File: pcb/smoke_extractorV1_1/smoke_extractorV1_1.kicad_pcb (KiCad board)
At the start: 2 copper layers, 54 x 27 mm, 43 parts, among them J1 USB_C_Receptacle, J2 Screw_Terminal_01x02, Q1 AO3400A, U1 LMV331, U2 RA11131100, U3 MP1542, U4 LMV331, U5 LMV331

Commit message: Version 1.2
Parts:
- added D6: SS34, Diode_SMD:Nexperia_CFP3_SOD-123W, F.Cu at (98.6, 111.5)
- added kibuzzard-631C7DF6: G***, kibuzzard-631C7DF6, F.Cu at (144.5, 107.0)
- added kibuzzard-631C7E0D: G***, kibuzzard-631C7E0D, F.Cu at (144.6, 112.0)
- R10: value 4k7 -> 5k1
- R12: value 86.6k -> 1k
- R17: value 10k -> 12k
- R18, R19, R6: value 4.7k -> 5k1
- R5: value 4.7k -> 47k
- R9: value 330 -> 100
- U1, U4, U5: footprint Package_TO_SOT_SMD:SOT-353_SC-70-5_Handsoldering -> Package_TO_SOT_SMD:SOT-23-5_HandSoldering
- moved R15 3.79 mm to (115.9, 98.6), turned to 90 degrees
- moved R8 0.91 mm to (94.6, 114.1), turned to -90 degrees
- moved R7 0.81 mm to (97.5, 115.0), turned to 0 degrees
- moved R9 0.45 mm to (107.0, 113.5)
- moved C7 0.21 mm to (119.7, 109.3)
- moved R14 0.06 mm to (117.8, 102.4)
- turned Q1 to 90 degrees
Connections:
- C1 pad 1: VBUS_RAW -> VBUS_OPEN
- C2 pad 2: GND -> VBUS_DRAIN
- C3 pad 2: GND -> VBUS_DRAIN
- C5 pad 2: GND -> VBUS_DRAIN
- C6 pad 1: VBUS_RAW -> VBUS_OPEN
- C7 pad 1: VBUS_RAW -> VBUS_OPEN
- D4 pad 1: GND -> VBUS_DRAIN
- J1 pad A4: VBUS_RAW -> VBUS_OPEN
- J1 pad A9: VBUS_RAW -> VBUS_OPEN
- J1 pad B4: VBUS_RAW -> VBUS_OPEN
- J1 pad B9: VBUS_RAW -> VBUS_OPEN
- J2 pad 2: GND -> VBUS_DRAIN
- Q1 pad 2: VBUS_OPEN -> GND
- Q1 pad 3: VBUS_RAW -> VBUS_DRAIN
- R1 pad 2: VBUS_RAW -> VBUS_OPEN
- R14 pad 2: GND -> VBUS_DRAIN
- R15 pad 2: GND -> VBUS_DRAIN
- R17 pad 2: GND -> VBUS_DRAIN
- R18 pad 2: VBUS_RAW -> VBUS_OPEN
- R19 pad 2: VBUS_RAW -> VBUS_OPEN
- R3 pad 2: VBUS_RAW -> VBUS_OPEN
- R6 pad 2: VBUS_RAW -> VBUS_OPEN
- R7 pad 2: VBUS_RAW -> VBUS_OPEN
- U1 pad 5: VBUS_RAW -> VBUS_OPEN
- U3 pad 4: GND -> VBUS_DRAIN
- U4 pad 5: VBUS_RAW -> VBUS_OPEN
- U5 pad 5: VBUS_RAW -> VBUS_OPEN
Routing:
- net VBUS_RAW: track 28.3 -> 0.00 mm, vias 3 -> 0
- net VBUS_OPEN: track 0.00 -> 24.6 mm, vias 0 -> 3
- net Net-(Q1-Pad1): track 0.00 -> 8.23 mm
- net V_CC_REF: track 40.9 -> 44.2 mm
- net CHG_DET: track 15.4 -> 16.4 mm
- net Net-(C4-Pad2): track 2.12 -> 2.72 mm
- net VBUS_DRAIN: vias 0 -> 28
- net GND: vias 162 -> 125
- added copper zone on B.Cu, net VBUS_DRAIN
- added copper zone on F.Cu, net VBUS_DRAIN
- removed copper zone on F.Cu, net Net-(Q1-Pad1)
- removed copper zone on F.Cu, net VBUS_RAW
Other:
- board text added: "Nuno Nogueira Stockholm Set 2022"
- board text added: "Smoke Extractor 1v2"
- board text removed: "Nuno Nogueira Stockholm July 2022"
- board text removed: "Smoke Extractor 1v1"

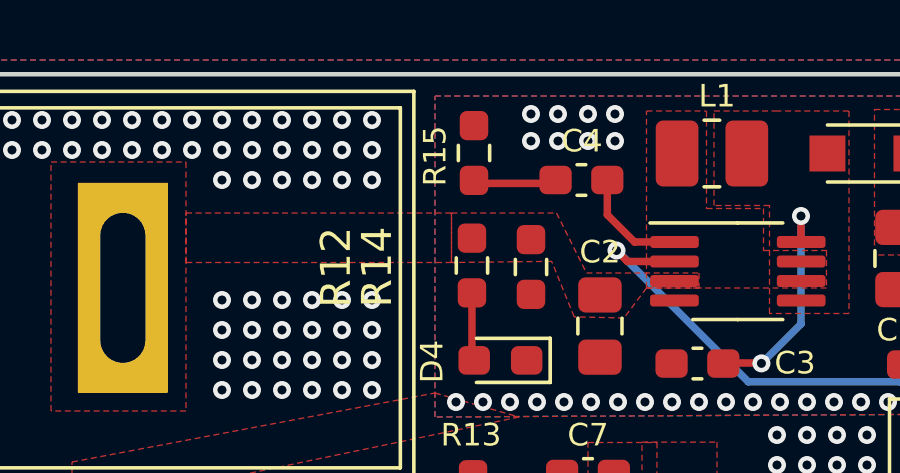
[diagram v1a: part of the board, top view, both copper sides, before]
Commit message: Added testing pads for version 1.2
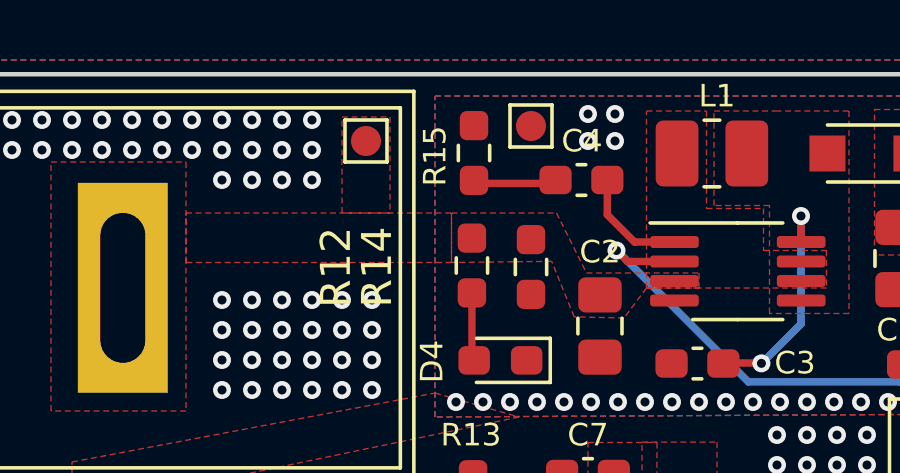
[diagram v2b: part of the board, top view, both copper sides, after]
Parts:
- added REF**: TestPoint_Pad_1.0x1.0mm, TestPoint:TestPoint_Pad_1.0x1.0mm, F.Cu at (112.3, 98.2)
- added REF**: TestPoint_Pad_1.0x1.0mm, TestPoint:TestPoint_Pad_1.0x1.0mm, F.Cu at (117.8, 97.7)
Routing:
- net VBUS_DRAIN: vias 28 -> 24
- net GND: vias 125 -> 119
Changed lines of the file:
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@@
     )
+  )
+  (footprint "TestPoint:TestPoint_Pad_1.0x1.0mm" (layer "F.Cu")
+    (at 112.3 98.2)
+    (descr "SMD rectangular pad as test Point, square 1.0mm side length")
+    (tags "test point SMD pad rectangle square")
+    (attr exclude_from_pos_files exclude_from_bom)
+    (fp_text reference "REF**" (at 0 -1.448) (layer "F.SilkS") hide
+      (effects (font (size 1 1) (thickness 0.15)))
+    )
+    (fp_text value "TestPoint_Pad_1.0x1.0mm" (at 0 1.55) (layer "F.Fab") hide
+      (effects (font (size 1 1) (thickness 0.15)))
+    )
+    (fp_text user "${REFERENCE}" (at 0 -1.45) (layer "F.Fab") hide
+      (effects (font (size 1 1) (thickness 0.15)))
+    )
+    (fp_line (start -0.7 0.7) (end -0.7 -0.7) (layer "F.SilkS") (width 0.12))
+    (fp_line (start 0.7 0.7) (end -0.7 0.7) (layer "F.SilkS") (width 0.12))
+    (fp_line (start -0.7 -0.7) (end 0.7 -0.7) (layer "F.SilkS") (width 0.12))
+    (fp_line (start 0.7 -0.7) (end 0.7 0.7) (layer "F.SilkS") (width 0.12))
+    (fp_line (start 1 1) (end -1 1) (layer "F.CrtYd") (width 0.05))
+    (fp_line (start 1 1) (end 1 -1) (layer "F.CrtYd") (width 0.05))
+    (fp_line (start -1 -1) (end 1 -1) (layer "F.CrtYd") (width 0.05))
+    (fp_line (start -1 -1) (end -1 1) (layer "F.CrtYd") (width 0.05))
+    (pad "1" smd circle (at 0 0) (size 1 1) (layers "F.Cu" "F.Mask")
+      (net 2 "VBUS_SWITCH") (zone_connect 2))
   )
   (footprint "Capacitor_SMD:C_0603_1608Metric_Pad1.08x0.95mm_HandSolder" locked (layer "F.Cu")
@@
     (attr board_only exclude_from_pos_files exclude_from_bom)
     (fp_text reference "kibuzzard-631C7E0D" (at 0 -3.511021 90) (layer "F.SilkS") hide
-      (effects (font (size 0 0)))
+      (effects (font (size 0 0) (thickness 0.15)))
     )
     (fp_text value "G***" (at 0 3.511021 90) (layer "F.SilkS") hide
-      (effects (font (size 0 0)))
+      (effects (font (size 0 0) (thickness 0.15)))
     )
     (fp_poly (pts
@@
     (attr board_only exclude_from_pos_files exclude_from_bom)
     (fp_text reference "kibuzzard-631C7DF6" (at 0 -3.511021 90) (layer "F.SilkS") hide
-      (effects (font (size 0 0)))
+      (effects (font (size 0 0) (thickness 0.15)))
     )
     (fp_text value "G***" (at 0 3.511021 90) (layer "F.SilkS") hide
-      (effects (font (size 0 0)))
+      (effects (font (size 0 0) (thickness 0.15)))
     )
     (fp_poly (pts
@@
     )
   )
+  (footprint "TestPoint:TestPoint_Pad_1.0x1.0mm" (layer "F.Cu")
+    (at 117.8 97.7)
+    (descr "SMD rectangular pad as test Point, square 1.0mm side length")
+    (tags "test point SMD pad rectangle square")
+    (attr exclude_from_pos_files exclude_from_bom)
+    (fp_text reference "REF**" (at 0 -1.448) (layer "F.SilkS") hide
+      (effects (font (size 1 1) (thickness 0.15)))
+    )
+    (fp_text value "TestPoint_Pad_1.0x1.0mm" (at 0 1.55) (layer "F.Fab") hide
+      (effects (font (size 1 1) (thickness 0.15)))
+    )
+    (fp_text user "${REFERENCE}" (at 0 -1.45) (layer "F.Fab") hide
+      (effects (font (size 1 1) (thickness 0.15)))
+    )
+    (fp_line (start 0.7 0.7) (end -0.7 0.7) (layer "F.SilkS") (width 0.12))
+    (fp_line (start -0.7 -0.7) (end 0.7 -0.7) (layer "F.SilkS") (width 0.12))
+    (fp_line (start -0.7 0.7) (end -0.7 -0.7) (layer "F.SilkS") (width 0.12))
+    (fp_line (start 0.7 -0.7) (end 0.7 0.7) (layer "F.SilkS") (width 0.12))
+    (fp_line (start 1 1) (end 1 -1) (layer "F.CrtYd") (width 0.05))
+    (fp_line (start -1 -1) (end 1 -1) (layer "F.CrtYd") (width 0.05))
+    (fp_line (start 1 1) (end -1 1) (layer "F.CrtYd") (width 0.05))
+    (fp_line (start -1 -1) (end -1 1) (layer "F.CrtYd") (width 0.05))
+    (pad "1" smd circle (at 0 0) (size 1 1) (layers "F.Cu" "F.Mask")
+      (net 24 "VBUS_DRAIN") (zone_connect 2))
+  )
   (footprint "Diode_SMD:D_SOD-523" locked (layer "F.Cu")
     (at 110.55 114.45)
@@
   (via locked (at 137.5 97.5) (size 0.6) (drill 0.3) (layers "F.Cu" "B.Cu") (free) (net 1))
   (via locked (at 108.5 103.5) (size 0.6) (drill 0.3) (layers "F.Cu" "B.Cu") (free) (net 1))
-  (via locked (at 112.5 99.5) (size 0.6) (drill 0.3) (layers "F.Cu" "B.Cu") (free) (net 1))
   (via locked (at 126 110) (size 0.6) (drill 0.3) (layers "F.Cu" "B.Cu") (free) (net 1))
   (via locked (at 103.5 98.5) (size 0.6) (drill 0.3) (layers "F.Cu" "B.Cu") (free) (net 1))
-  (via locked (at 111.5 98.5) (size 0.6) (drill 0.3) (layers "F.Cu" "B.Cu") (free) (net 1))
   (via locked (at 139.5 102.5) (size 0.6) (drill 0.3) (layers "F.Cu" "B.Cu") (free) (net 1))
   (via locked (at 136.5 114) (size 0.6) (drill 0.3) (layers "F.Cu" "B.Cu") (free) (net 1))
@@
   (via locked (at 137.5 99.5) (size 0.6) (drill 0.3) (layers "F.Cu" "B.Cu") (free) (net 1))
   (via locked (at 109.5 99.5) (size 0.6) (drill 0.3) (layers "F.Cu" "B.Cu") (free) (net 1))
-  (via locked (at 112.5 97.5) (size 0.6) (drill 0.3) (layers "F.Cu" "B.Cu") (free) (net 1))
   (via locked (at 129 109) (size 0.6) (drill 0.3) (layers "F.Cu" "B.Cu") (free) (net 1))
   (via locked (at 127 110) (size 0.6) (drill 0.3) (layers "F.Cu" "B.Cu") (free) (net 1))
@@
   (via locked (at 138.5 98.5) (size 0.6) (drill 0.3) (layers "F.Cu" "B.Cu") (free) (net 1))
   (via locked (at 94 111.6) (size 0.6) (drill 0.3) (layers "F.Cu" "B.Cu") (free) (net 1))
-  (via locked (at 111.5 97.5) (size 0.6) (drill 0.3) (layers "F.Cu" "B.Cu") (free) (net 1))
   (via locked (at 128 114) (size 0.6) (drill 0.3) (layers "F.Cu" "B.Cu") (free) (net 1))
   (via locked (at 126 112) (size 0.6) (drill 0.3) (layers "F.Cu" "B.Cu") (free) (net 1))
@@
   (via locked (at 138.5 99.5) (size 0.6) (drill 0.3) (layers "F.Cu" "B.Cu") (free) (net 1))
   (via locked (at 128 111) (size 0.6) (drill 0.3) (layers "F.Cu" "B.Cu") (free) (net 1))
-  (via locked (at 112.5 98.5) (size 0.6) (drill 0.3) (layers "F.Cu" "B.Cu") (free) (net 1))
   (via locked (at 122.5 120) (size 0.6) (drill 0.3) (layers "F.Cu" "B.Cu") (free) (net 1))
   (via locked (at 108.5 106.5) (size 0.6) (drill 0.3) (layers "F.Cu" "B.Cu") (free) (net 1))
   (via locked (at 126 109) (size 0.6) (drill 0.3) (layers "F.Cu" "B.Cu") (free) (net 1))
   (via locked (at 94 110.6) (size 0.6) (drill 0.3) (layers "F.Cu" "B.Cu") (free) (net 1))
-  (via locked (at 111.5 99.5) (size 0.6) (drill 0.3) (layers "F.Cu" "B.Cu") (free) (net 1))
   (via locked (at 112.5 104.5) (size 0.6) (drill 0.3) (layers "F.Cu" "B.Cu") (free) (net 1))
   (via locked (at 136.5 113) (size 0.6) (drill 0.3) (layers "F.Cu" "B.Cu") (free) (net 1))
@@
   (via locked (at 126.1 106.9) (size 0.6) (drill 0.3) (layers "F.Cu" "B.Cu") (free) (net 24))
   (via locked (at 124.3 106.9) (size 0.6) (drill 0.3) (layers "F.Cu" "B.Cu") (free) (net 24))
-  (via locked (at 118.7 97.3) (size 0.6) (drill 0.3) (layers "F.Cu" "B.Cu") (free) (net 24))
   (via locked (at 130.6 106.9) (size 0.6) (drill 0.3) (layers "F.Cu" "B.Cu") (free) (net 24))
   (via locked (at 125.2 106.9) (size 0.6) (drill 0.3) (layers "F.Cu" "B.Cu") (free) (net 24))
@@
   (via locked (at 115.3 106.9) (size 0.6) (drill 0.3) (layers "F.Cu" "B.Cu") (free) (net 24))
   (via locked (at 122.5 106.9) (size 0.6) (drill 0.3) (layers "F.Cu" "B.Cu") (free) (net 24))
-  (via locked (at 118.7 98.2) (size 0.6) (drill 0.3) (layers "F.Cu" "B.Cu") (free) (net 24))
   (via locked (at 119.8 106.9) (size 0.6) (drill 0.3) (layers "F.Cu" "B.Cu") (free) (net 24))
   (via locked (at 120.6 98.2) (size 0.6) (drill 0.3) (layers "F.Cu" "B.Cu") (free) (net 24))
-  (via locked (at 117.8 98.2) (size 0.6) (drill 0.3) (layers "F.Cu" "B.Cu") (free) (net 24))
-  (via locked (at 117.8 97.3) (size 0.6) (drill 0.3) (layers "F.Cu" "B.Cu") (free) (net 24))
   (via locked (at 128.8 106.9) (size 0.6) (drill 0.3) (layers "F.Cu" "B.Cu") (free) (net 24))
   (via locked (at 127 106.9) (size 0.6) (drill 0.3) (layers "F.Cu" "B.Cu") (free) (net 24))
@@
       )
     )
+  )
+  (zone (net 2) (net_name "VBUS_SWITCH") (layer "F.Cu") (hatch edge 0.508)
+    (priority 4)
+    (connect_pads (clearance 0.15))
+    (min_thickness 0.254) (filled_areas_thickness no)
+    (fill yes (thermal_gap 0.508) (thermal_bridge_width 0.508))
+    (polygon
+      (pts
+        (xy 113.1 100.6)
+        (xy 111.5 100.6)
+        (xy 111.5 97.4)
+        (xy 113.1 97.4)
+      )
+    )
